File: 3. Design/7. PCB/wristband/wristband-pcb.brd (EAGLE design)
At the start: 27.5 x 36.3 mm, 44 parts, among them IC1 STM32F051K8T6, Y2 FA-20H_16.0000MF12Z-AC3, Y3 FA-20H_16.0000MF12Z-AC3

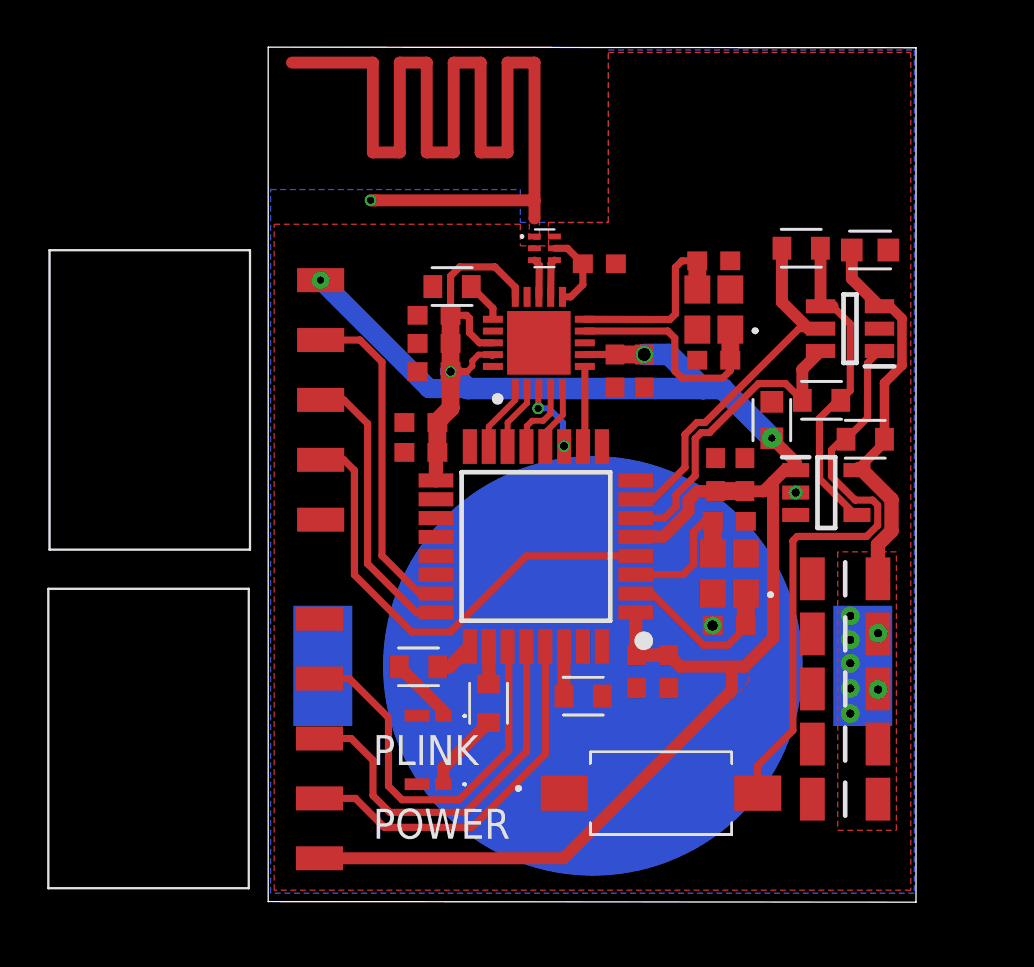
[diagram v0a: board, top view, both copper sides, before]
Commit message: UPDT: Almost all 3D models applied in the wristband pcb
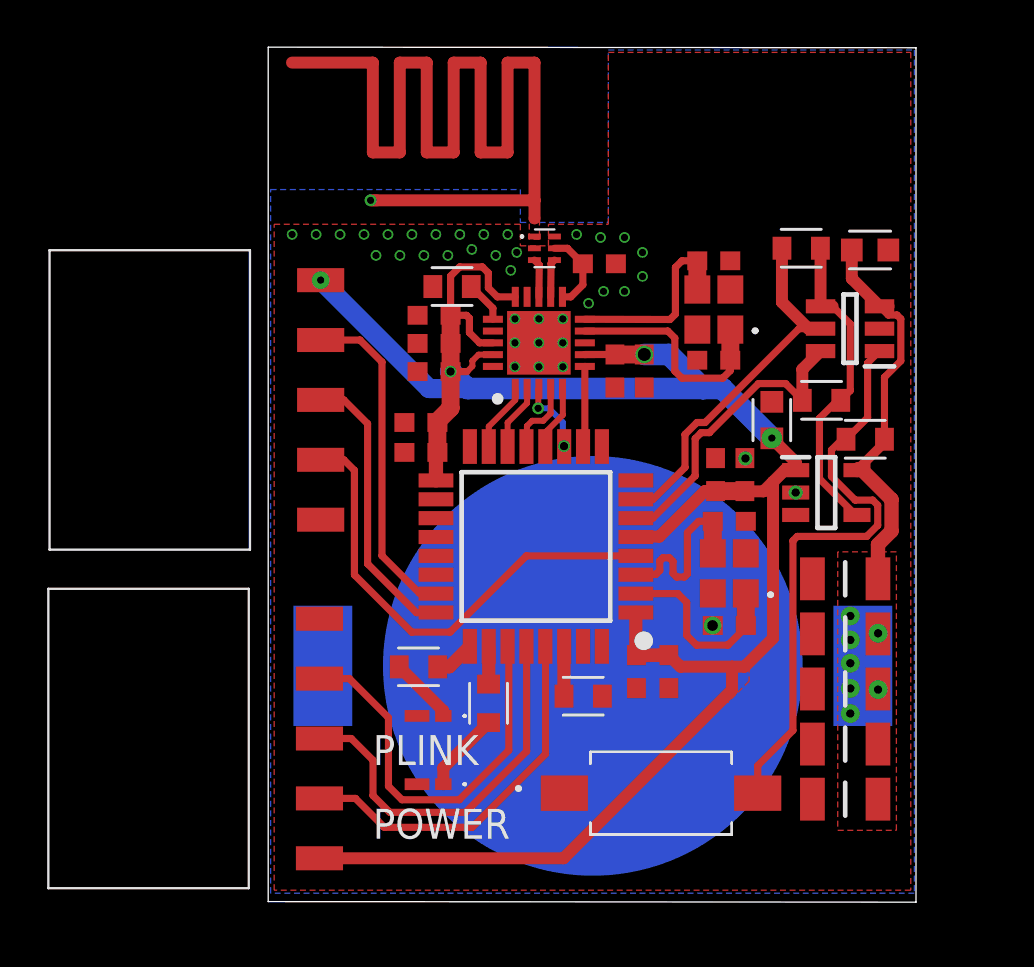
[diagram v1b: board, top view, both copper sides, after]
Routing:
- net STM32F051_CRYSTAL2: track 6.36 -> 7.80 mm
- net STM32F051_CRYSTAL1: track 7.32 -> 8.13 mm
- net GND: vias 3 -> 39

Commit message: ADD|UPDT: Exported new and corrected old 3D models, 2D models and technical drawings of all  PCBs
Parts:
- moved ANT1 0.91 mm to (11.7, 27.5)
- moved BATT_HLD 0.91 mm to (13.8, 9.74)
- moved C1 0.91 mm to (21.4, 20.2)
- moved C10 0.91 mm to (24.5, 8.76)
- moved C11 0.91 mm to (24.5, 13.4)
- moved C12 0.91 mm to (24.5, 11.1)
- moved C14 0.91 mm to (24.5, 6.43)
- moved C15 0.91 mm to (18.9, 22.7)
- moved C16 0.91 mm to (18.9, 26.9)
- moved C17 0.91 mm to (19.6, 11.5)
- moved C18 0.91 mm to (19.6, 15.9)
- moved C19 0.91 mm to (6.48, 18.8)
- moved C2 0.91 mm to (25.5, 27.4)
- moved C20 0.91 mm to (17.0, 9.50)
- moved C21 0.91 mm to (15.6, 9.50)
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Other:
- board size 27.5 x 36.3 mm -> 27.5 x 36 mm
- board text added: "."
- board text added: "Hugo C. José M."

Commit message: ADD: pb-switch and wristband CAM files
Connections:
- net N$4: now also IC1.31; no longer IC1.30
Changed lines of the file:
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@@
 <signal name="N$4">
 <contactref element="R7" pad="1"/>
-<contactref element="IC1" pad="30"/>
-<wire x1="12.5538" y1="10.5702" x2="12.5452" y2="10.5616" width="0.5588" layer="1"/>
-<wire x1="12.5452" y1="10.5616" x2="12.5452" y2="8.4582" width="0.5588" layer="1"/>
+<contactref element="IC1" pad="31"/>
+<wire x1="13.3538" y1="10.5702" x2="13.3538" y2="9.2668" width="0.6096" layer="1"/>
+<wire x1="13.3538" y1="9.2668" x2="12.5452" y2="8.4582" width="0.6096" layer="1"/>
 </signal>
 <signal name="FLG">

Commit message: Project at the time of delivery
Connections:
- net N$4: now also IC1.30; no longer IC1.31
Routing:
- net N$4: track 2.45 -> 1.14 mm
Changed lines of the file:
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@@
 <drawing>
 <settings>
-<setting alwaysvectorfont="yes"/>
+<setting alwaysvectorfont="no"/>
 <setting verticaltext="up"/>
 </settings>
@@
 </layers>
 <board>
-<fusionsync huburn="a.YnVzaW5lc3M6YWx1bm9zNjU4" projecturn="a.YnVzaW5lc3M6YWx1bm9zNjU4I0QyMDIwMTEyNjM1NzA0MDM1MQ" f3durn="urn:adsk.wipprod:dm.lineage:bKpgsLsdQMqy66-_QmCFMA" pcbguid="" lastpulledtime="2020-12-20T21:33:40Z" lastsyncedchangeguid="" latestrevisionid="9daa5ef3-dd75-4898-81f4-dd43f1275c59" lastsyncedrevisionid="9daa5ef3-dd75-4898-81f4-dd43f1275c59" lastboardhashguid="ac83953b-309a-8dae-37b7-7914f2571517" lastpushedtime="2020-12-20T22:28:16Z" linktopcb3d="true"/>
+<fusionsync huburn="a.YnVzaW5lc3M6YWx1bm9zNjU4" projecturn="a.YnVzaW5lc3M6YWx1bm9zNjU4I0QyMDIwMTEyNjM1NzA0MDM1MQ" f3durn="urn:adsk.wipprod:dm.lineage:bKpgsLsdQMqy66-_QmCFMA" pcbguid="" lastpulledtime="2020-12-20T21:33:40Z" lastsyncedchangeguid="" latestrevisionid="9daa5ef3-dd75-4898-81f4-dd43f1275c59" lastsyncedrevisionid="9daa5ef3-dd75-4898-81f4-dd43f1275c59" lastboardhashguid="ac83953b-309a-8dae-37b7-7914f2571517" lastpushedtime="2020-12-20T22:28:16Z" linktopcb3d="false"/>
 <plain>
 <text x="4.445" y="2.413" size="1.27" layer="21" font="vector" ratio="16">POWER</text>
@@
 <signal name="N$4">
 <contactref element="R7" pad="1"/>
-<contactref element="IC1" pad="31"/>
-<wire x1="13.3538" y1="10.5702" x2="13.3538" y2="9.2668" width="0.6096" layer="1"/>
 <wire x1="13.3538" y1="9.2668" x2="12.5452" y2="8.4582" width="0.6096" layer="1"/>
+<contactref element="IC1" pad="30"/>
+<wire x1="13.3538" y1="9.2668" x2="12.5538" y2="10.5702" width="0" layer="19" extent="1-1"/>
 </signal>
 <signal name="FLG">
